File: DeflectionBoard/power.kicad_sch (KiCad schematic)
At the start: 27 parts, among them J101 Conn_01x02, U101 TPS55340PWPR, U102 AP63205WU, U103 REF3325AIDCKT

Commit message: DeflectionBoard: channel X + power schematic complete, ERC clean
Full-bridge hysteretic current-mode deflection channel (CSD97394Q4M),
INA240 current sense, OPA2196 input scale, TLV3501 comparator, EN pull-up.
Power: TPS55340 boost (R106=78.7k/~600kHz), AP63205 buck 5V, REF3325 Vmid.
Hierarchical: root + Power + Deflection_Channel sheets, AXIS_IN sheet pin
wired to input connector. 0 ERC violations.

Co-Authored-By: Claude Opus 4.8 <noreply@anthropic.com>
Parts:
- added R106: 78.7K, symbol Device:R_Small
- U101: footprint vectrex repro:PWP14 -> PWP14
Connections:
- net GND: now also U101.15 (EPAD), U101.6 (SYNC), R106.1
- net at D102.2 (A), L101.2, U101.1 (SW): now also U101.2 (SW)
- net at U101.10 (FREQ): now also R106.2
- net +2.5V renamed +2V5
- no-connect marks 4 -> 0
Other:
- moved on the sheet: U103

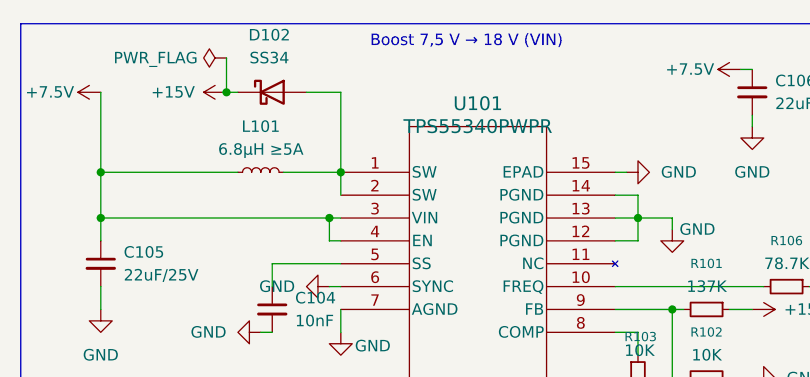
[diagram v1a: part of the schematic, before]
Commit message: DeflectionBoard: channel Y instanced, footprints assigned, ERC clean
- Y axis = 2nd instance of Deflection_Channel sheet (X=2xx, Y=3xx)
- Signal labels made local (per-instance scoping), power refs uniquified
- Footprints: 0402 passives, R201/R301 shunt=2512, D102=SS54/SMB,
  J1=PH 4p / J101=VH power / yoke=XH (keyed), L101=12x12 / L102=SRN6045
- E96 1% feedback/timing resistors (137k/53.6k/78.7k)

Co-Authored-By: Claude Opus 4.8 <noreply@anthropic.com>
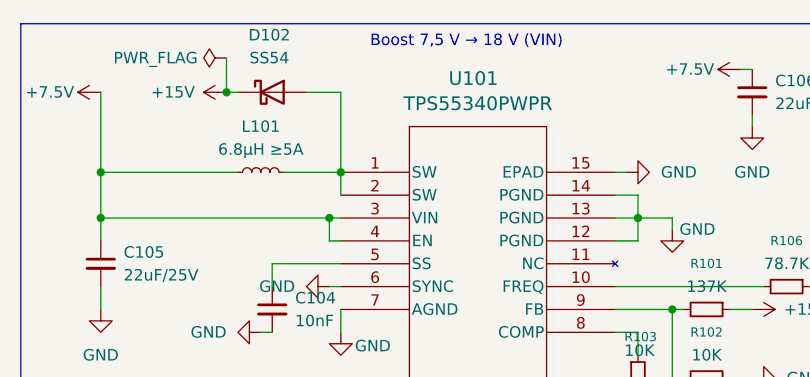
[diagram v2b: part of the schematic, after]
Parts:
- C101: footprint (none) -> Capacitor_SMD:CP_Elec_6.3x7.7
- C102, C110, C111: footprint (none) -> Capacitor_SMD:C_0805_2012Metric
- C103, C104, C109, C112, C113, C114: footprint (none) -> Capacitor_SMD:C_0402_1005Metric
- C105, C106, C107, C108: footprint (none) -> Capacitor_SMD:C_1206_3216Metric
- D102: value SS34 -> SS54; footprint (none) -> Diode_SMD:D_SMB
- J101: footprint (none) -> Connector_JST:JST_VH_B2P-VH-B_1x02_P3.96mm_Vertical
- L101: footprint (none) -> Inductor_SMD:L_12x12mm_H6mm
- L102: footprint (none) -> Inductor_SMD:L_Bourns_SRN6045TA
- R101, R102, R103, R104, R105, R106: footprint (none) -> Resistor_SMD:R_0402_1005Metric
- U101: footprint PWP14 -> vectrex repro:PWP14
- U103: footprint DCK3 -> vectrex repro:DCK3
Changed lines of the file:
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@@
 			)
 		)
-		(property "Footprint" ""
+		(property "Footprint" "Inductor_SMD:L_12x12mm_H6mm"
 			(at 123.19 35.56 0)
 			(hide yes)
@@
 			)
 		)
-		(property "Footprint" ""
+		(property "Footprint" "Capacitor_SMD:C_0402_1005Metric"
 			(at 50.8 96.52 0)
 			(hide yes)
@@
 			)
 		)
-		(property "Value" "SS34"
+		(property "Value" "SS54"
 			(at 124.1425 22.86 0)
 			(show_name no)
@@
 			)
 		)
-		(property "Footprint" ""
+		(property "Footprint" "Diode_SMD:D_SMB"
 			(at 124.46 31.115 0)
 			(hide yes)
@@
 			)
 		)
-		(property "Footprint" ""
+		(property "Footprint" "Resistor_SMD:R_0402_1005Metric"
 			(at 165.1 58.42 0)
 			(hide yes)
@@
 			)
 		)
-		(property "Footprint" ""
+		(property "Footprint" "Capacitor_SMD:C_0805_2012Metric"
 			(at 217.17 27.94 0)
 			(hide yes)
@@
 			)
 		)
-		(property "Footprint" ""
+		(property "Footprint" "Capacitor_SMD:C_0402_1005Metric"
 			(at 147.32 66.04 0)
 			(hide yes)
@@
 			)
 		)
-		(property "Footprint" ""
+		(property "Footprint" "Resistor_SMD:R_0402_1005Metric"
 			(at 172.72 50.8 0)
 			(hide yes)
@@
 			)
 		)
-		(property "Footprint" ""
+		(property "Footprint" "Capacitor_SMD:C_0402_1005Metric"
 			(at 265.43 44.45 0)
 			(hide yes)
@@
 			)
 		)
-		(property "Footprint" ""
+		(property "Footprint" "Capacitor_SMD:CP_Elec_6.3x7.7"
 			(at 39.37 31.75 0)
 			(hide yes)
@@
 			)
 		)
-		(property "Footprint" ""
+		(property "Footprint" "Capacitor_SMD:C_0402_1005Metric"
 			(at 124.46 50.8 0)
 			(hide yes)
@@
 			)
 		)
-		(property "Footprint" ""
+		(property "Footprint" "Capacitor_SMD:C_0805_2012Metric"
 			(at 217.17 59.69 0)
 			(hide yes)
@@
 			)
 		)
-		(property "Footprint" ""
+		(property "Footprint" "Capacitor_SMD:C_1206_3216Metric"
 			(at 177.8 26.67 0)
 			(hide yes)
@@
 			)
 		)
-		(property "Footprint" ""
+		(property "Footprint" "Capacitor_SMD:C_1206_3216Metric"
 			(at 115.57 66.04 0)
 			(hide yes)
@@
 			)
 		)
-		(property "Footprint" ""
+		(property "Footprint" "Capacitor_SMD:C_0805_2012Metric"
 			(at 55.88 31.75 0)
 			(hide yes)
@@
 			)
 		)
-		(property "Footprint" ""
+		(property "Footprint" "Inductor_SMD:L_Bourns_SRN6045TA"
 			(at 257.81 35.56 0)
 			(hide yes)
@@
 			)
 		)
-		(property "Datasheet" ""
+		(property "Datasheet" "SRN6045-3R3Y"
 			(at 257.81 35.56 0)
 			(hide yes)
@@
 			)
 		)
-		(property "Footprint" ""
+		(property "Footprint" "Resistor_SMD:R_0402_1005Metric"
 			(at 181.61 48.26 0)
 			(hide yes)
@@
 			)
 		)
-		(property "Footprint" ""
+		(property "Footprint" "Connector_JST:JST_VH_B2P-VH-B_1x02_P3.96mm_Vertical"
 			(at 27.94 25.4 0)
 			(hide yes)
@@
 			)
 		)
-		(property "Footprint" "DCK3"
+		(property "Footprint" "vectrex repro:DCK3"
 			(at 46.99 83.82 0)
 			(hide yes)
@@
 			)
 		)
-		(property "Footprint" ""
+		(property "Footprint" "Resistor_SMD:R_0402_1005Metric"
 			(at 172.72 58.42 0)
 			(hide yes)
@@
 			)
 		)
-		(property "Footprint" ""
+		(property "Footprint" "Capacitor_SMD:C_1206_3216Metric"
 			(at 130.81 66.04 0)
 			(hide yes)
@@
 			)
 		)
-		(property "Footprint" ""
+		(property "Footprint" "Capacitor_SMD:C_0402_1005Metric"
 			(at 165.1 66.04 0)
 			(hide yes)
@@
 			)
 		)
-		(property "Footprint" ""
+		(property "Footprint" "Resistor_SMD:R_0402_1005Metric"
 			(at 265.43 52.07 0)
 			(hide yes)
@@
 			)
 		)
-		(property "Footprint" ""
+		(property "Footprint" "Capacitor_SMD:C_0402_1005Metric"
 			(at 35.56 96.52 0)
 			(hide yes)
@@
 		(in_pos_files yes)
 		(dnp no)
-		(fields_autoplaced yes)
 		(property "Reference" "U101"
-			(at 147.32 27.94 0)
+			(at 146.812 25.146 0)
 			(show_name no)
 			(do_not_autoplace no)
@@
 		)
 		(property "Value" "TPS55340PWPR"
-			(at 147.32 30.48 0)
+			(at 147.32 27.94 0)
 			(show_name no)
 			(do_not_autoplace no)
@@
 			)
 		)
-		(property "Footprint" "PWP14"
+		(property "Footprint" "vectrex repro:PWP14"
 			(at 132.08 35.56 0)
 			(hide yes)
@@
 			)
 		)
-		(property "Footprint" ""
+		(property "Footprint" "Capacitor_SMD:C_1206_3216Metric"
 			(at 105.41 45.72 0)
 			(hide yes)
@@
 			)
 		)
-		(property "Footprint" ""
+		(property "Footprint" "Resistor_SMD:R_0402_1005Metric"
 			(at 255.27 52.07 0)
 			(hide yes)
